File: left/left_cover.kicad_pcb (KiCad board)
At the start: 2 copper layers, 117.6 x 97.9 mm, 22 parts, among them J1 USB_C_Receptacle_IN, J2 USB_C_Receptacle_OUT, SW1 SW_Push, SW2 SW_SPDT

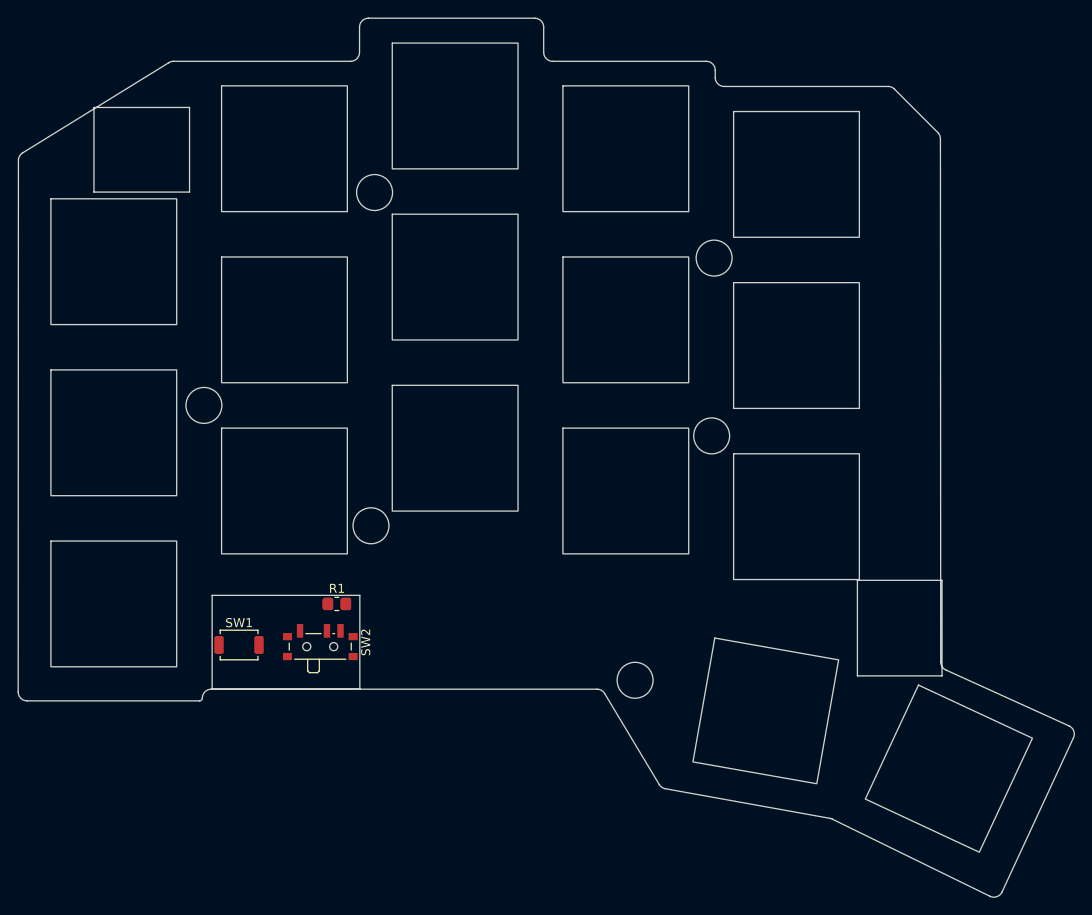
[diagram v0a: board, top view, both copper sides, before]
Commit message: modified edge cut
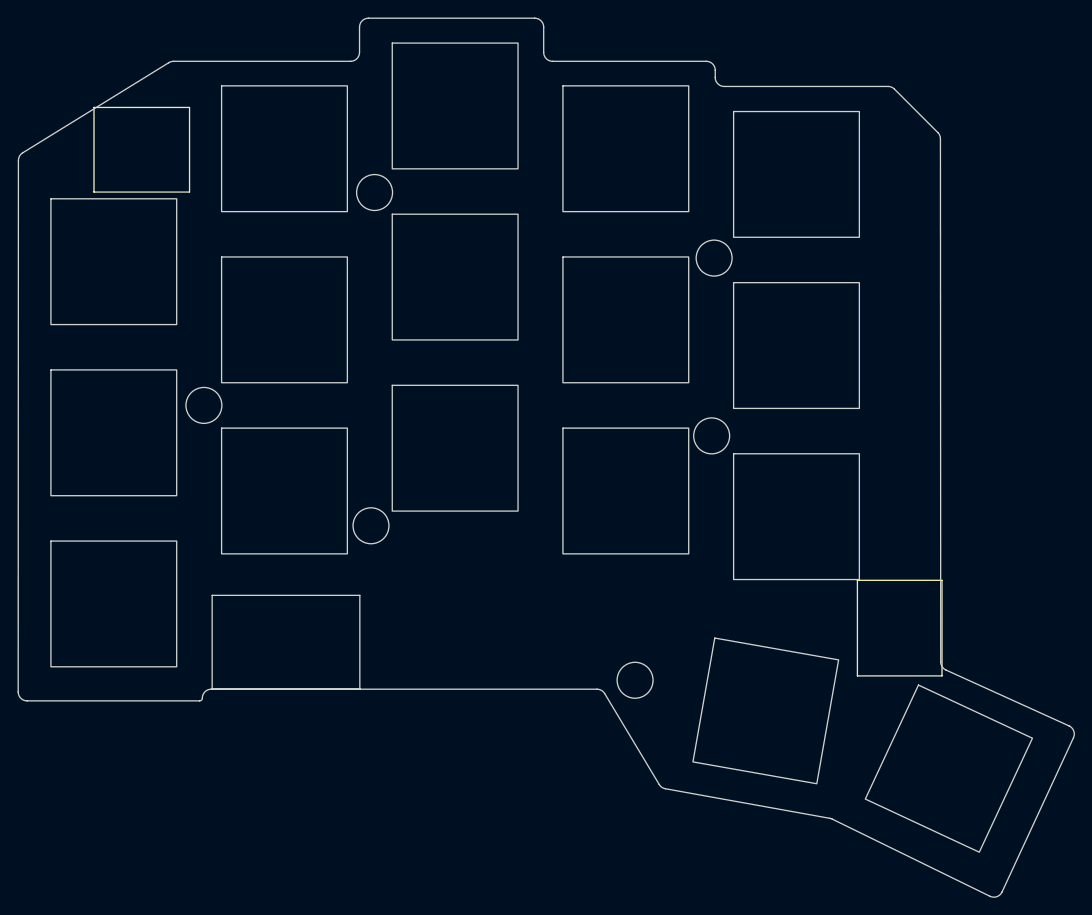
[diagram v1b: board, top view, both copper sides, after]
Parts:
- removed R1: 10k, Resistor_SMD:R_0805_2012Metric_Pad1.20x1.40mm_HandSolder
- removed SW1: SW_Push, Button_Switch_SMD:SW_SPST_TS-1088-xR020
- removed SW2: SW_SPDT, Button_Switch_SMD:SW_SPDT_PCM12
